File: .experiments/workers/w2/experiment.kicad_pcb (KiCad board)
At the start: 2 copper layers, 140 x 90 mm, 39 parts, among them J1 USB_C, J2 Output, J3 Debug, Q1 FS8205A, U1 USBLC6-2SC6, U2 BQ24072, U3 HY2113-KB5B, U4 MT3608, U5 AP2112K-3.3, U6 LN61CN3302MR-G

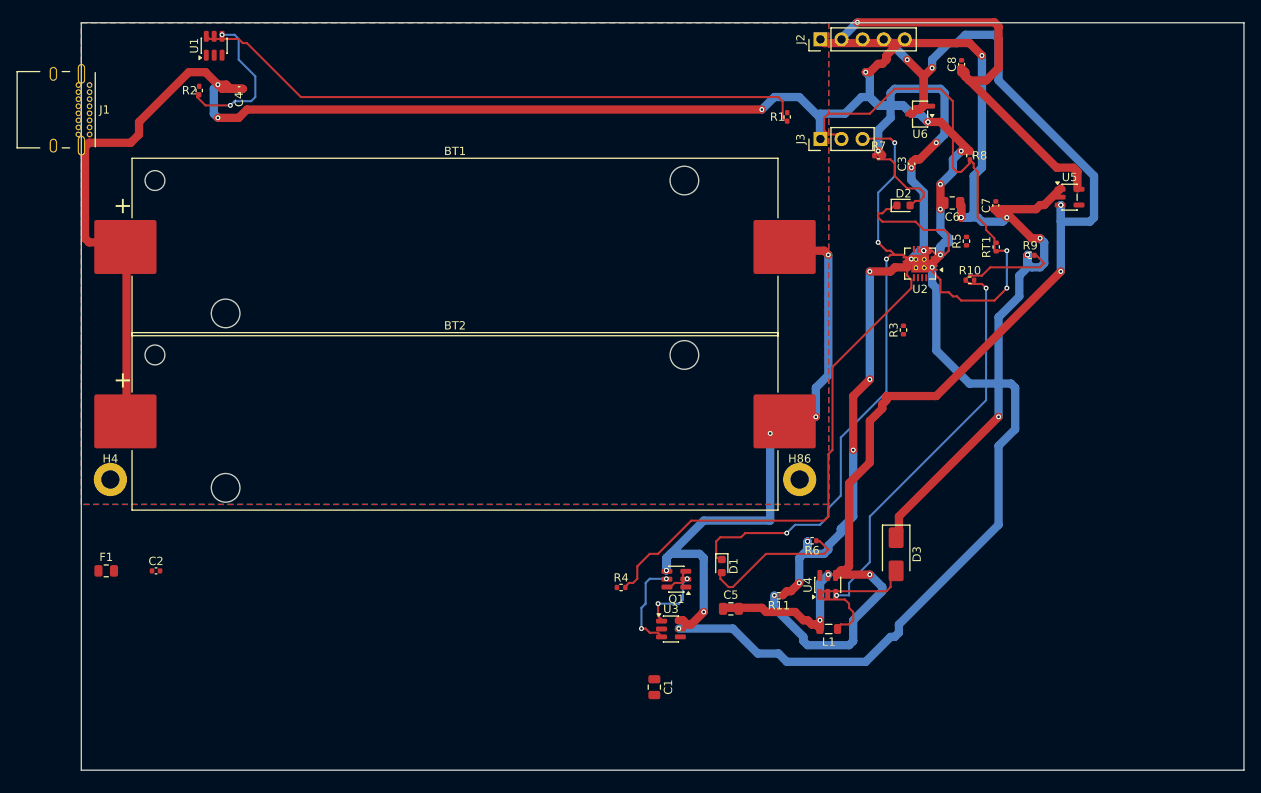
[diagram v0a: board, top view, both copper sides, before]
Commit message: 35-round experiment: best score 25.33, improved routing params
Router and conflict resolution tuning from autonomous optimization loop.
Best config: clearance=0.2051mm, cooling_factor=0.9735, existing_trace_cost=200.0

Co-Authored-By: Claude Opus 4.6 <noreply@anthropic.com>
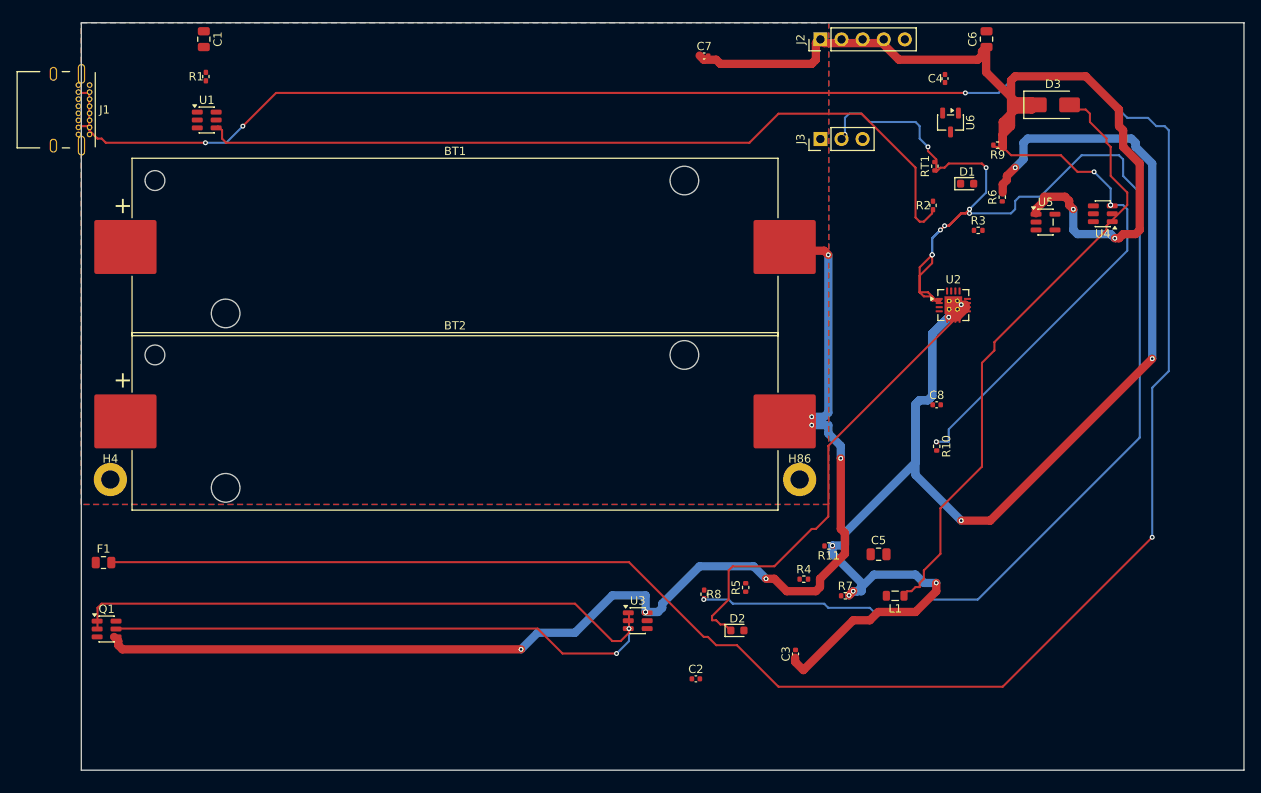
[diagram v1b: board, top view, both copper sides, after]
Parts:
- moved C1 95.0 mm to (14.8, 1.97)
- moved R2 89.4 mm to (102.6, 22.0)
- moved C4 85.0 mm to (104.0, 6.71), turned to 90 degrees
- moved R1 70.2 mm to (15.0, 6.48)
- moved Q1 68.9 mm to (3.04, 73.0), turned to 0 degrees
- moved C2 66.3 mm to (74.0, 79.0)
- moved R8 61.8 mm to (75.0, 68.8)
- moved C3 60.6 mm to (86.0, 76.0)
- moved D3 57.3 mm to (117.0, 9.88), turned to 0 degrees
- moved U4 55.6 mm to (123.0, 23.0), turned to 180 degrees
- moved D2 54.9 mm to (79.0, 73.2)
- moved D1 54.7 mm to (106.7, 19.4), turned to 0 degrees
- moved R7 53.2 mm to (92.0, 69.0)
- moved R5 49.5 mm to (80.0, 68.0)
- moved R6 47.3 mm to (110.9, 21.0), turned to 90 degrees
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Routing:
- net Net-(F1-Pad2): track 0.00 -> 332.1 mm, vias 0 -> 4
- net /VBAT: track 293.0 -> 0.00 mm, vias 14 -> 0
- net /EN: track 149.0 -> 0.00 mm, vias 8 -> 0
- net /NTC_SENSE: track 62.8 -> 181.7 mm, vias 2 -> 10
- net /VSYS: track 93.0 -> 191.6 mm, vias 12 -> 10
- net Net-(R2-Pad1): track 18.4 -> 98.7 mm, vias 2 -> 0
- net /CELL_NEG: track 75.5 -> 152.7 mm, vias 6 -> 8
- net Net-(R1-Pad1): track 75.5 -> 0.00 mm
- net /CHG_N: track 75.4 -> 0.00 mm, vias 4 -> 0
- net Net-(Q1A-G): track 8.12 -> 71.5 mm, vias 2 -> 0
- net Net-(U2-ILIM): track 62.7 -> 0.00 mm
- net Net-(D3-A): track 19.7 -> 74.5 mm
- net Net-(Q1B-G): track 11.3 -> 65.4 mm
- net /3V3: track 52.5 -> 0.00 mm, vias 2 -> 0
- net Net-(D2-K): track 18.7 -> 54.9 mm
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
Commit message: 45-round experiment: best score 25.66, all nets routed (26/26)
Fixed A* performance by increasing max_search from 100k->500k to handle
high trace costs (100.0) without timing out. Kept high cost + coarse grid
(0.5mm) to prevent shorts while still routing efficiently.

Best config: edge_margin=5.7493mm, cooling_factor=0.9764, existing_trace_cost=200, max_rips=8

Co-Authored-By: Claude Opus 4.6 <noreply@anthropic.com>
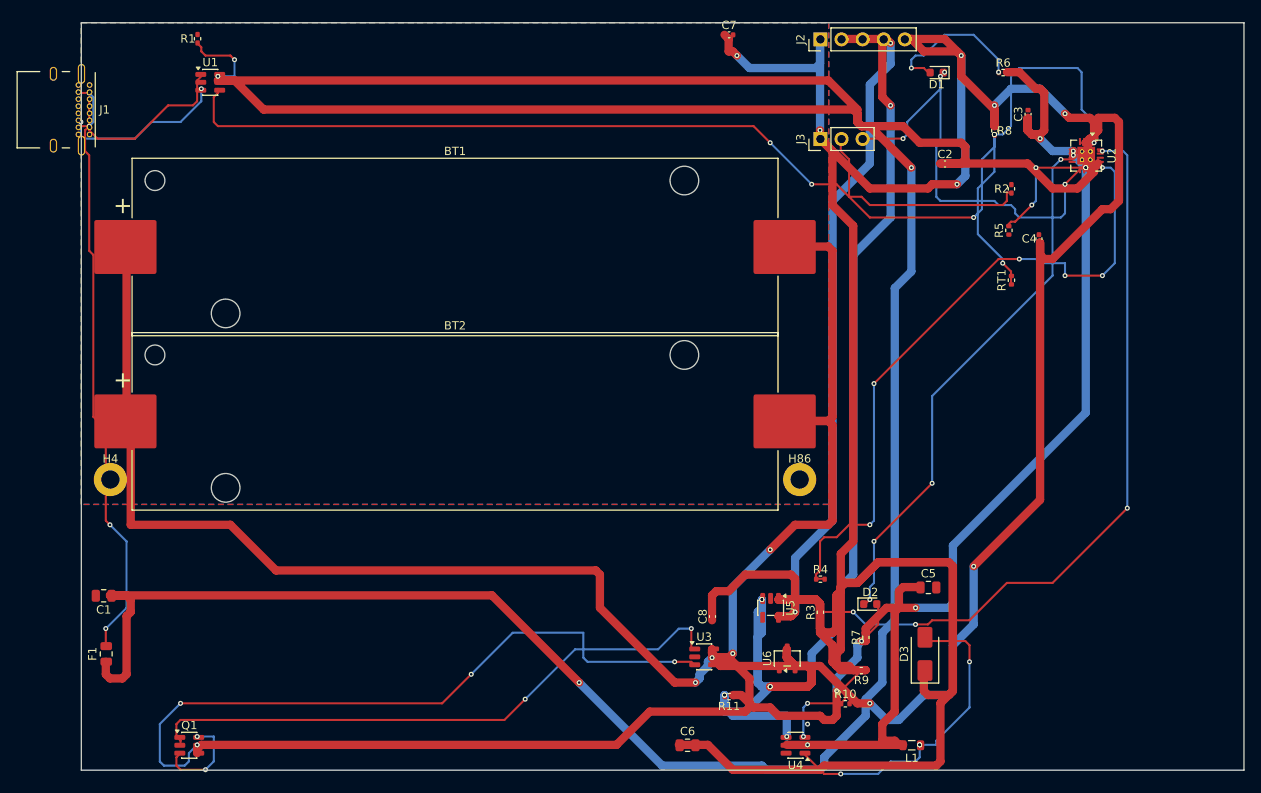
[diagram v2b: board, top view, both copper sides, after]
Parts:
- moved C6 92.3 mm to (73.0, 87.0), turned to 0 degrees
- moved U4 73.9 mm to (86.0, 87.0)
- moved C3 70.8 mm to (114.0, 11.0)
- moved C2 68.9 mm to (104.0, 17.0)
- moved C1 68.1 mm to (2.69, 69.0), turned to 180 degrees
- moved D3 67.9 mm to (101.6, 76.0), turned to 90 degrees
- moved U6 67.5 mm to (85.0, 76.5), turned to 90 degrees
- moved R8 65.9 mm to (110.0, 13.0)
- moved R9 65.4 mm to (93.9, 78.0)
- moved U5 57.0 mm to (83.0, 70.5), turned to -90 degrees
- moved R5 53.4 mm to (111.7, 25.0)
- moved R3 49.8 mm to (89.0, 71.0), turned to 90 degrees
- moved C8 37.1 mm to (76.0, 71.5), turned to 90 degrees
- moved R10 32.9 mm to (92.0, 82.0), turned to 0 degrees
- moved U2 24.1 mm to (121.0, 16.0), turned to -90 degrees
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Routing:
- net /VBUS: track 0.00 -> 396.7 mm, vias 0 -> 2
- net /VBAT: track 0.00 -> 319.7 mm, vias 0 -> 9
- net Net-(F1-Pad2): track 332.1 -> 72.2 mm
- net /EN: track 0.00 -> 154.2 mm, vias 0 -> 8
- net /5V: track 114.7 -> 256.4 mm, vias 2 -> 4
- net /3V3: track 0.00 -> 102.1 mm, vias 0 -> 2
- net /NTC_SENSE: track 181.7 -> 81.6 mm, vias 10 -> 6
- net Net-(U2-ISET): track 0.00 -> 89.8 mm, vias 0 -> 4
- net Net-(U2-ILIM): track 0.00 -> 81.0 mm, vias 0 -> 6
- net /VSYS: track 191.6 -> 122.2 mm, vias 10 -> 8
- net /CHG_N: track 0.00 -> 53.8 mm, vias 0 -> 4
- net Net-(U4-FB): track 58.7 -> 13.0 mm, vias 4 -> 2
- net /VSYS_BOOST: track 0.00 -> 38.2 mm
- net Net-(D3-A): track 74.5 -> 38.9 mm, vias 0 -> 4
- net Net-(J1-CC1): track 0.00 -> 22.5 mm
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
